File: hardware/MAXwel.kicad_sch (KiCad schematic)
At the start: 155 parts, among them J1 Conn_02x05_Odd_Even, J2 Conn_02x12_Counter_Clockwise, J3 Barrel_Jack_Switch_Pin3Ring, SW1 SW_Push_Dual, SW10 SW_Wuerth_450301014042, SW11 SW_Wuerth_450301014042, SW12 SW_Wuerth_450301014042, SW13 SW_Wuerth_450301014042, SW2 SW_Push_Dual, SW3 SW_Push_Dual, SW4 SW_Push_Dual, SW5 SW_Wuerth_450301014042, SW6 SW_Wuerth_450301014042, SW7 SW_Wuerth_450301014042, SW8 SW_Wuerth_450301014042, SW9 SW_Push_DPDT, U1 D168K, U2 D168K, U3 D168K, U4 D168K, U5 EPM240T100, U6 AMS1117-3.3, X1 50.000, X2 14.756

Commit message: README: project status update
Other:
- note removed: "TODO: Bauteil-Nummer und Footprint bei allen Kondensatoren in diesem Schaltplan"
- note removed: "TODO: Prüfen, ob Prog. Header richtig angeschlossen Pin 10 mit GND Verbidung richtig?"
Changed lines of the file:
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@@
-		)
-	)
-	(text "TODO: Prüfen, ob Prog. Header richtig angeschlossen\nPin 10 mit GND Verbidung richtig?"
-		(exclude_from_sim no)
-		(at 251.46 172.466 0)
-		(effects
-			(font
-				(size 1.27 1.27)
-			)
 		)
 	)
@@
 		(effects
 			(font
-				(size 1.27 1.27)
-			)
-		)
-	)
-	(text "TODO: Bauteil-Nummer und Footprint bei allen Kondensatoren in diesem Schaltplan"
-		(exclude_from_sim no)
-		(at 222.504 177.546 0)
-		(effects
-			(font

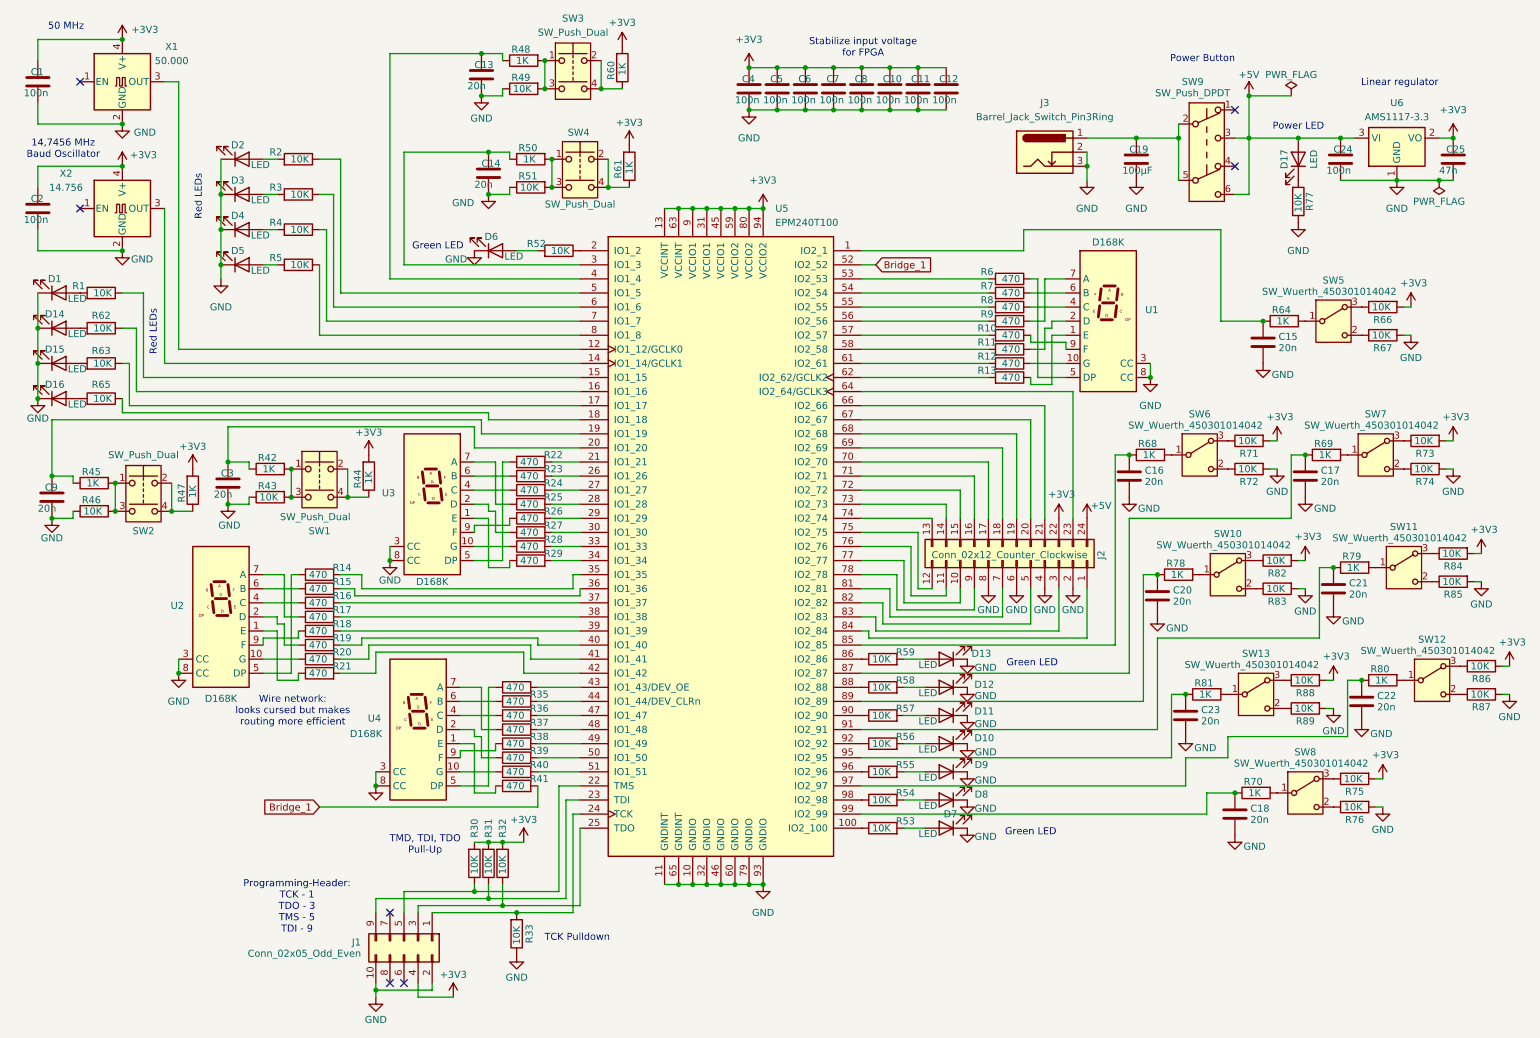
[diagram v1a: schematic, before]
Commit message: removed resistors at sliding switches, 5mm smaller circuit board
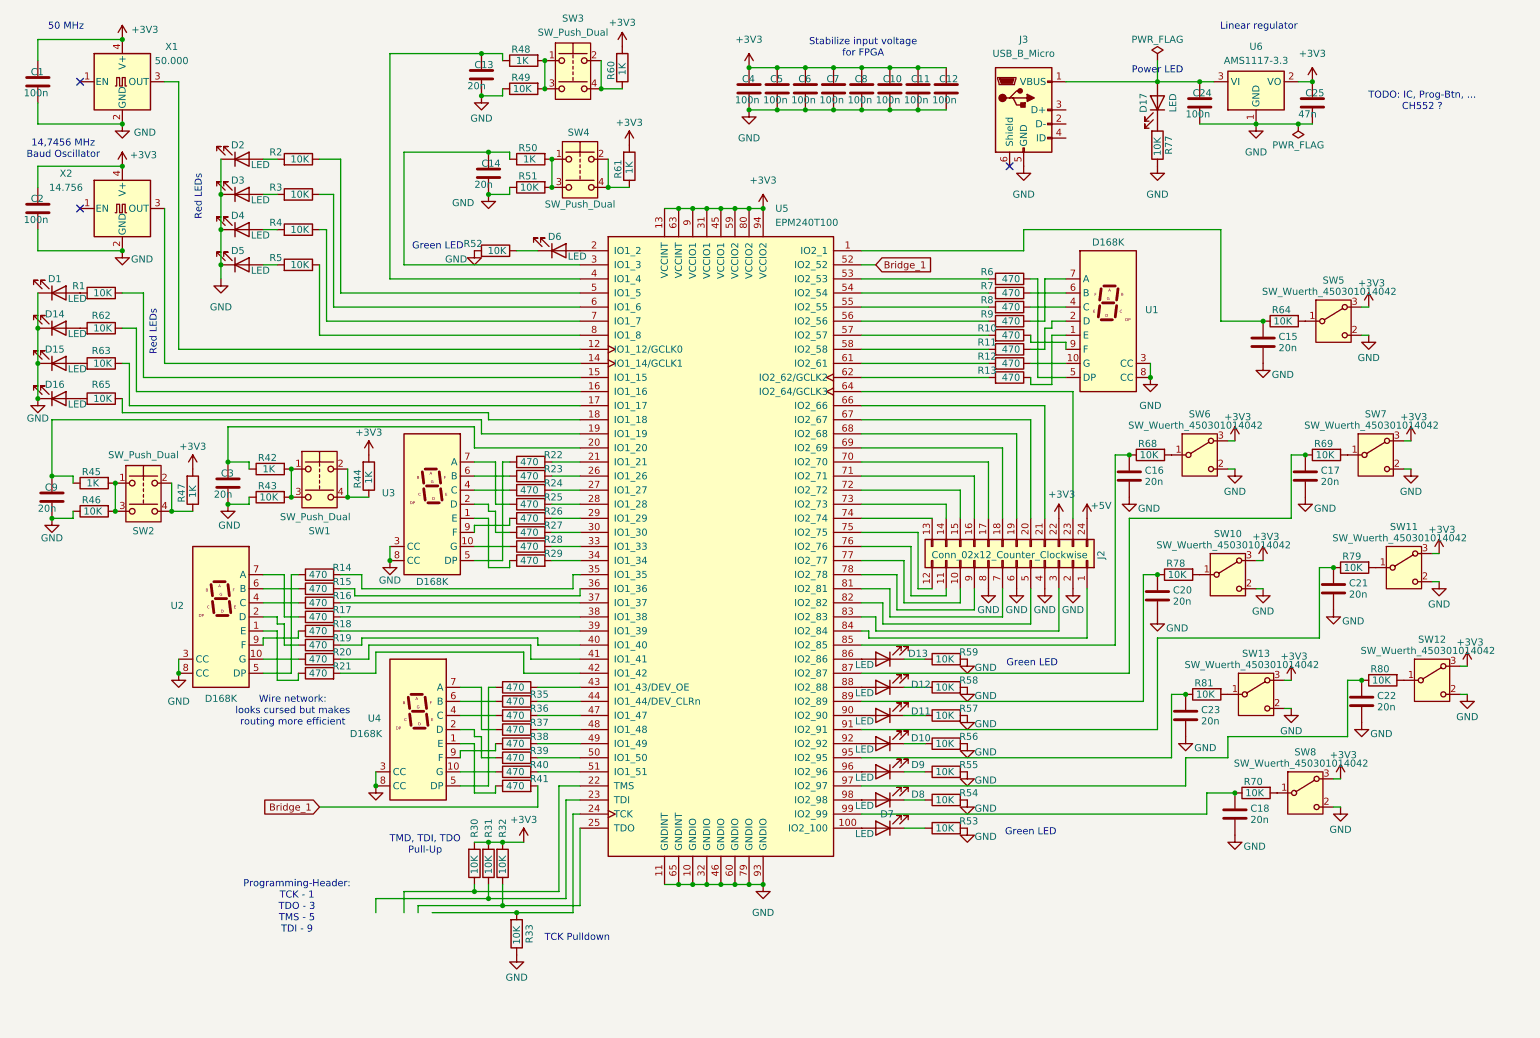
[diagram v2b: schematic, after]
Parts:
- removed C19: 100µF, Capacitor_THT:CP_Radial_D5.0mm_P2.00mm, symbol Device:C
- removed J1: Conn_02x05_Odd_Even, Connector_IDC:IDC-Header_2x05_P2.54mm_Vertical, symbol Connector_Generic:Conn_02x05_Odd_Even
- removed J3: Barrel_Jack_Switch_Pin3Ring, Connector_BarrelJack:BarrelJack_Horizontal, symbol Connector:Barrel_Jack_Switch_Pin3Ring
- removed R66, R67, R71, R72, R73, R74, R75, R76, R82, R83, R84, R85, R86, R87, R88, R89: 10K, Resistor_SMD:R_0603_1608Metric_Pad0.98x0.95mm_HandSolder, symbol Device:R
- removed SW9: SW_Push_DPDT, Button_Switch_THT:SW_Push_2P2T_Toggle_CK_PVA2OAH5xxxxxxV2, symbol Switch:SW_Push_DPDT
- added J3: USB_B_Micro, Connector_USB:USB_Micro-B_Molex_47346-0001, symbol Connector:USB_B_Micro
- R64, R68, R69, R70, R78, R79, R80, R81: value 1K -> 10K
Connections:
- net +3V3: now also SW10.3 (A), SW11.3 (A), SW12.3 (A), SW13.3 (A), SW5.3 (A), SW6.3 (A), SW7.3 (A), SW8.3 (A)
- net +5V: no longer C24.1, D17.2 (A), U6.3 (VI)
- net GND: now also R52.2, R53.2, R54.2, R55.2, R56.2, R57.2, R58.2, R59.2, SW10.2 (C), SW11.2 (C), SW12.2 (C), SW13.2 (C), SW5.2 (C), SW6.2 (C), SW7.2 (C), SW8.2 (C), J3.5 (GND); no longer D10.1 (K), D11.1 (K), D12.1 (K), D13.1 (K), D6.1 (K), D7.1 (K), D8.1 (K), D9.1 (K)
- net at R59.1: now also D13.1 (K); no longer U5.86 (IO2_86)
- net at D13.2 (A): now also U5.86 (IO2_86); no longer R59.2
- net at U5.100 (IO2_100): now also D7.2 (A); no longer R53.1
- net at U5.2 (IO1_2): now also D6.2 (A); no longer R52.1
- net at U5.88 (IO2_88): now also D12.2 (A); no longer R58.1
- net at U5.90 (IO2_90): now also D11.2 (A); no longer R57.1
- net at U5.92 (IO2_92): now also D10.2 (A); no longer R56.1
- net at U5.96 (IO2_96): now also D9.2 (A); no longer R55.1
- net at U5.98 (IO2_98): now also D8.2 (A); no longer R54.1
- new net: D6.1 (K), R52.1
- new net: D9.1 (K), R55.1
- new net: C24.1, D17.2 (A), J3.1 (VBUS), U6.3 (VI)
- new net: D7.1 (K), R53.1
- new net: D11.1 (K), R57.1
- new net: D8.1 (K), R54.1
- new net: D12.1 (K), R58.1
- new net: D10.1 (K), R56.1
- no-connect marks 7 -> 3
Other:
- note added: "TODO: IC, Prog-Btn, ... CH552 ?"
- note removed: "Power Button"
- moved on the sheet: C24, C25, D10, D11, D12, D13, D17, D6, D7, D8, D9, R52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
